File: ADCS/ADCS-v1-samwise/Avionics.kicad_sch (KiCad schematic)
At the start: 42 parts, among them SW1 KMR231NG LFS, SW2 KMR231NG LFS, U2 RP2350_80QFN, U3 MR25H40MDF, Y1 ABM8-272-T3

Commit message: ver 1.5
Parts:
- removed D4: LED, LED_SMD:LED_0603_1608Metric, symbol Device:LED
- removed TP13: TestPoint, TestPoint:TestPoint_Pad_D1.0mm, symbol Connector:TestPoint
- added D5: GREEN LED, LED_SMD:LED_0603_1608Metric, symbol Device:LED
- R70: value 650 -> 10k
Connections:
- net GND: now also D5.1 (K)
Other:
- note removed: "Vwd: 2V Ifwd: 2mA R = (3.3-2)/2mA = 650Ω"
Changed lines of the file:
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@@
 		(title "ADCS Main Board")
 		(date "2025-05-21")
-		(rev "1.4")
+		(rev "1.5")
 		(company "Stanford Student Space Initiative")
 		(comment 1 "Sage Wu")
@@
 		)
 	)
-	(text "Vwd: 2V\nIfwd: 2mA\nR = (3.3-2)/2mA\n= 650Ω"
-		(exclude_from_sim no)
-		(at 53.848 37.338 0)
-		(effects
-			(font
-				(size 1.27 1.27)
-			)
-			(justify left)
-		)
-	)
 	(text "capacitor for every power pin\n"
 		(exclude_from_sim no)
@@
 	)
 	(junction
+		(at 67.31 60.96)
+		(diameter 0)
+		(color 0 0 0 0)
+	)
+	(junction
 		(at 158.75 54.61)
 		(diameter 0)
@@
 	(wire
 		(pts
-			(xy 67.31 62.23) (xy 67.31 59.69)
+			(xy 67.31 62.23) (xy 67.31 60.96)
 		)
 		(stroke
@@
 	(wire
 		(pts
-			(xy 102.87 46.99) (xy 102.87 54.61)
-		)
-		(stroke
-			(width 0)
-			(type default)
-		)
-	)
-	(wire
-		(pts
 			(xy 143.51 158.75) (xy 147.32 158.75)
 		)
@@
 	(wire
 		(pts
+			(xy 67.31 60.96) (xy 67.31 59.69)
+		)
+		(stroke
+			(width 0)
+			(type default)
+		)
+	)
+	(wire
+		(pts
 			(xy 69.85 156.21) (xy 74.93 156.21)
 		)
@@
 	(wire
 		(pts
+			(xy 102.87 46.99) (xy 102.87 54.61)
+		)
+		(stroke
+			(width 0)
+			(type default)
+		)
+	)
+	(wire
+		(pts
 			(xy 143.51 143.51) (xy 147.32 143.51)
 		)
@@
 		)
 	)
+	(global_label "3V3_TEST"
+		(shape bidirectional)
+		(at 102.87 46.99 180)
+		(fields_autoplaced yes)
+		(effects
+			(font
+				(size 1.27 1.27)
+			)
+			(justify right)
+		)
+		(property "Intersheetrefs" "${INTERSHEET_REFS}"
+			(at 90.8176 46.99 0)
+			(effects
+				(font
+					(size 1.27 1.27)
+				)
+				(justify right)
+				(hide yes)
+			)
+		)
+	)
 	(global_label "pd_z+_1"
 		(shape input)
@@
 	)
 	(symbol
+		(lib_id "Device:LED")
+		(at 67.31 57.15 270)
+		(mirror x)
+		(unit 1)
+		(exclude_from_sim no)
+		(in_bom yes)
+		(on_board yes)
+		(dnp no)
+		(property "Reference" "D5"
+			(at 72.4154 57.3278 0)
+			(effects
+				(font
+					(size 1.27 1.27)
+				)
+			)
+		)
+		(property "Value" "GREEN LED"
+			(at 70.3072 57.3278 0)
+			(effects
+				(font
+					(size 0.9906 0.9906)
+				)
+			)
+		)
+		(property "Footprint" "LED_SMD:LED_0603_1608Metric"
+			(at 67.31 57.15 0)
+			(effects
+				(font
+					(size 1.27 1.27)
+				)
+				(hide yes)
+			)
+		)
+		(property "Datasheet" "https://optoelectronics.liteon.com/upload/download/DS22-2000-074/LTST-C190KGKT.PDF"
+			(at 67.31 57.15 0)
+			(effects
+				(font
+					(size 1.27 1.27)
+				)
+				(hide yes)
+			)
+		)
+		(property "Description" "Green LED"
+			(at 67.31 57.15 0)
+			(effects
+				(font
+					(size 1.27 1.27)
+				)
+				(hide yes)
+			)
+		)
+		(property "Flight" "LTST-C190KGKT"
+			(at 67.31 57.15 0)
+			(effects
+				(font
+					(size 1.27 1.27)
+				)
+				(hide yes)
+			)
+		)
+		(property "Manufacturer_Name" "Lite-On Inc."
+			(at 67.31 57.15 0)
+			(effects
+				(font
+					(size 1.27 1.27)
+				)
+				(hide yes)
+			)
+		)
+		(property "Manufacturer_Part_Number" "LTST-C190KGKT"
+			(at 74.9554 57.3278 0)
+			(effects
+				(font
+					(size 1.27 1.27)
+				)
+				(hide yes)
+			)
+		)
+		(property "Proto" "LTST-C190KGKT"
+			(at 67.31 57.15 0)
+			(effects
+				(font
+					(size 1.27 1.27)
+				)
+				(hide yes)
+			)
+		)
+		(property "Sim.Pins" "1=K 2=A"
+			(at 67.31 57.15 0)
+			(effects
+				(font
+					(size 1.27 1.27)
+				)
+			)
+		)
+		(pin "1"
+		)
+		(pin "2"
+		)
+		(instances
+			(project "ADCS_board"
+				(path "/db20b18b-d25a-428e-8229-70a189e1de75/00000000-0000-0000-0000-00005cec5a72"
+					(reference "D5")
+					(unit 1)
+				)
+			)
+		)
+	)
+	(symbol
 		(lib_id "Device:C_Small")
 		(at 34.29 100.33 0)
@@
 	)
 	(symbol
-		(lib_id "Connector:TestPoint")
-		(at 102.87 46.99 0)
-		(unit 1)
-		(exclude_from_sim no)
-		(in_bom no)
-		(on_board yes)
-		(dnp no)
-		(fields_autoplaced yes)
-		(property "Reference" "TP13"
-			(at 105.41 42.4179 0)
-			(effects
-				(font
-					(size 1.27 1.27)
-				)
-				(justify left)
-			)
-		)
-		(property "Value" "TestPoint"
-			(at 105.41 44.9579 0)
-			(effects
-				(font
-					(size 1.27 1.27)
-				)
-				(justify left)
-			)
-		)
-		(property "Footprint" "TestPoint:TestPoint_Pad_D1.0mm"
-			(at 107.95 46.99 0)
-			(effects
-				(font
-					(size 1.27 1.27)
-				)
-				(hide yes)
-			)
-		)
-		(property "Datasheet" "~"
-			(at 107.95 46.99 0)
-			(effects
-				(font
-					(size 1.27 1.27)
-				)
-				(hide yes)
-			)
-		)
-		(property "Description" "test point"
-			(at 102.87 46.99 0)
-			(effects
-				(font
-					(size 1.27 1.27)
-				)
-				(hide yes)
-			)
-		)
-		(pin "1"
-		)
-		(instances
-			(project "ADCS_board"
-				(path "/db20b18b-d25a-428e-8229-70a189e1de75/00000000-0000-0000-0000-00005cec5a72"
-					(reference "TP13")
-					(unit 1)
-				)
-			)
-		)
-	)
-	(symbol
 		(lib_id "Device:R_US")
 		(at 43.18 193.04 90)
@@
 			)
 		)
-		(property "Value" "650"
+		(property "Value" "10k"
 			(at 69.85 49.5299 0)
 			(effects
@@
 					(unit 1)
 				)
-			)
-		)
-	)
-	(symbol
-		(lib_id "Device:LED")
-		(at 67.31 55.88 90)
-		(unit 1)
-		(exclude_from_sim no)
-		(in_bom yes)
-		(on_board yes)
-		(dnp no)
-		(fields_autoplaced yes)
-		(property "Reference" "D4"
-			(at 71.12 56.1974 90)
-			(effects
-				(font
-					(size 1.27 1.27)
-				)
-				(justify right)
-			)
-		)
-		(property "Value" "LED"
-			(at 71.12 58.7374 90)
-			(effects
-				(font
-					(size 1.27 1.27)
-				)
-				(justify right)
-			)
-		)
-		(property "Footprint" "LED_SMD:LED_0603_1608Metric"
-			(at 67.31 55.88 0)
-			(effects
-				(font
-					(size 1.27 1.27)
-				)
-				(hide yes)
-			)
-		)
-		(property "Datasheet" "~"
-			(at 67.31 55.88 0)
-			(effects
-				(font
-					(size 1.27 1.27)
-				)
-				(hide yes)
-			)
-		)
-		(property "Description" "Light emitting diode"
-			(at 67.31 55.88 0)
-			(effects
-				(font
-					(size 1.27 1.27)
-				)
-				(hide yes)
-			)
-		)
-		(property "Sim.Pins" "1=K 2=A"
-			(at 67.31 55.88 0)
-			(effects
-				(font
-					(size 1.27 1.27)
-				)
-				(hide yes)
-			)
-		)
-		(pin "1"
-		)
-		(pin "2"
-		)
-		(instances
-			(project ""
-				(path "/db20b18b-d25a-428e-8229-70a189e1de75/00000000-0000-0000-0000-00005cec5a72"
-					(reference "D4")
-					(unit 1)
-				)

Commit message: ADCS v1.7
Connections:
- net at D5.2 (A): now also R70.1
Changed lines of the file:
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@@
 		(title "ADCS Main Board")
 		(date "2025-05-22")
-		(rev "1.6")
+		(rev "1.7")
 		(company "Stanford Student Space Initiative")
 		(comment 1 "Sage Wu")
@@
 	)
 	(junction
-		(at 67.31 60.96)
-		(diameter 0)
-		(color 0 0 0 0)
-	)
-	(junction
 		(at 158.75 54.61)
 		(diameter 0)
@@
 	(wire
 		(pts
+			(xy 67.31 60.96) (xy 67.31 63.5)
+		)
+		(stroke
+			(width 0)
+			(type default)
+		)
+	)
+	(wire
+		(pts
 			(xy 364.49 66.04) (xy 364.49 58.42)
 		)
@@
 	(wire
 		(pts
-			(xy 67.31 62.23) (xy 67.31 60.96)
-		)
-		(stroke
-			(width 0)
-			(type default)
-		)
-	)
-	(wire
-		(pts
 			(xy 118.11 80.01) (xy 120.65 80.01)
 		)
@@
 	(wire
 		(pts
-			(xy 80.01 38.1) (xy 80.01 41.91)
-		)
-		(stroke
-			(width 0)
-			(type default)
-		)
-	)
-	(wire
-		(pts
 			(xy 74.93 99.06) (xy 63.5 99.06)
 		)
@@
 	(wire
 		(pts
-			(xy 67.31 60.96) (xy 67.31 59.69)
-		)
-		(stroke
-			(width 0)
-			(type default)
-		)
-	)
-	(wire
-		(pts
 			(xy 69.85 156.21) (xy 74.93 156.21)
 		)
@@
 	(wire
 		(pts
+			(xy 80.01 35.56) (xy 80.01 41.91)
+		)
+		(stroke
+			(width 0)
+			(type default)
+		)
+	)
+	(wire
+		(pts
 			(xy 323.85 116.84) (xy 323.85 114.3)
 		)
@@
 	(wire
 		(pts
+			(xy 67.31 52.07) (xy 67.31 53.34)
+		)
+		(stroke
+			(width 0)
+			(type default)
+		)
+	)
+	(wire
+		(pts
 			(xy 336.55 173.99) (xy 336.55 177.8)
 		)
@@
 		)
 	)
-	(global_label "3V3_TEST"
+	(global_label "3.3V"
 		(shape bidirectional)
 		(at 102.87 46.99 180)
@@
 		)
 		(property "Intersheetrefs" "${INTERSHEET_REFS}"
-			(at 90.8176 46.99 0)
+			(at 95.4741 46.99 0)
 			(effects
 				(font
@@
 			)
 		)
-		(property "Datasheet" "https://optoelectronics.liteon.com/upload/download/DS22-2000-074/LTST-C190KGKT.PDF"
+		(property "Datasheet" "~"
 			(at 67.31 57.15 0)
 			(effects
@@
 			)
 		)
-		(property "Description" "Green LED"
+		(property "Description" "Light emitting diode"
 			(at 67.31 57.15 0)
 			(effects
@@
 		)
 		(property "Sim.Pins" "1=K 2=A"
-			(at 67.31 57.15 0)
+			(at 64.77 55.118 0)
 			(effects
 				(font
@@
 	(symbol
 		(lib_id "power:+3.3V")
-		(at 80.01 38.1 0)
+		(at 80.01 35.56 0)
 		(unit 1)
 		(exclude_from_sim no)
@@
 		(fields_autoplaced yes)
 		(property "Reference" "#P+04"
-			(at 80.01 38.1 0)
+			(at 80.01 35.56 0)
 			(effects
 				(font
@@
 		)
 		(property "Value" "3.3V"
-			(at 80.01 33.02 0)
+			(at 80.01 30.48 0)
 			(effects
 				(font
@@
 		)
 		(property "Footprint" ""
-			(at 80.01 38.1 0)
+			(at 80.01 35.56 0)
 			(effects
 				(font
@@
 		)
 		(property "Datasheet" ""
-			(at 80.01 38.1 0)
+			(at 80.01 35.56 0)
 			(effects
 				(font
@@
 		)
 		(property "Description" "Power symbol creates a global label with name \"+3.3V\""
-			(at 80.01 38.1 0)
+			(at 80.01 35.56 0)
 			(effects
 				(font
@@
 	(symbol
 		(lib_id "power:GND")
-		(at 67.31 62.23 0)
+		(at 67.31 63.5 0)
 		(unit 1)
 		(exclude_from_sim no)
@@
 		(fields_autoplaced yes)
 		(property "Reference" "#PWR088"
-			(at 67.31 68.58 0)
+			(at 67.31 69.85 0)
 			(effects
 				(font
@@
 		)
 		(property "Value" "GND"
-			(at 67.31 67.31 0)
+			(at 67.31 68.58 0)
 			(effects
 				(font
@@
 		)
 		(property "Footprint" ""
-			(at 67.31 62.23 0)
+			(at 67.31 63.5 0)
 			(effects
 				(font
@@
 		)
 		(property "Datasheet" ""
-			(at 67.31 62.23 0)
+			(at 67.31 63.5 0)
 			(effects
 				(font
@@
 		)
 		(property "Description" "Power symbol creates a global label with name \"GND\" , ground"
-			(at 67.31 62.23 0)
+			(at 67.31 63.5 0)
 			(effects
 				(font

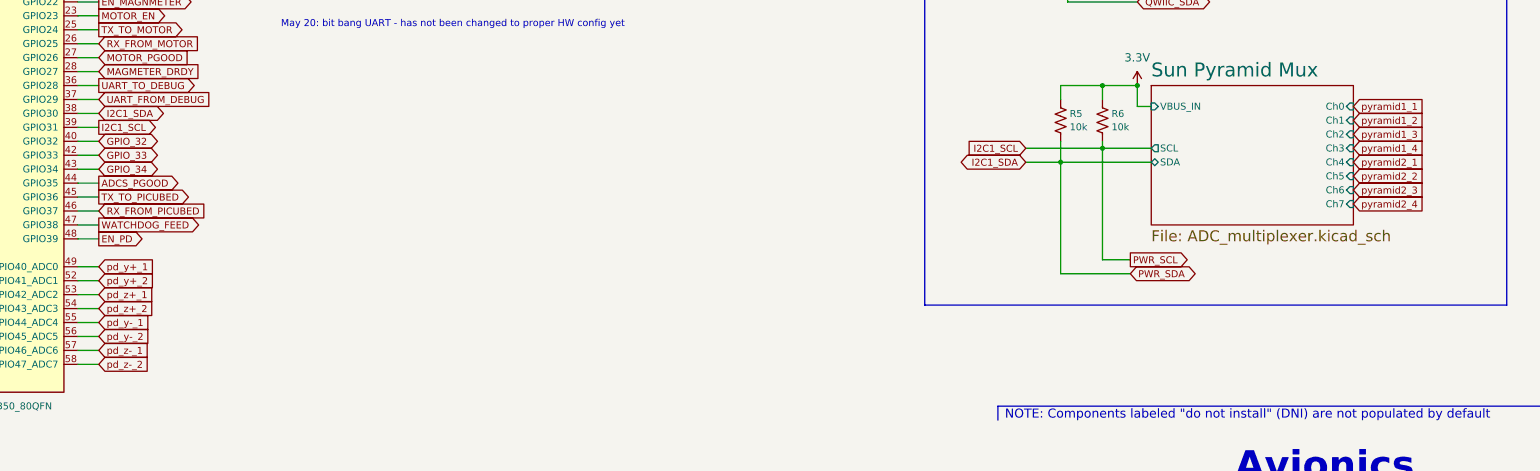
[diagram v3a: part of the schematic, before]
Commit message: Swap sun pyramid / photodiode yz inputs
Swap sun pyramid / photodiode yz inputs
 - Sun pyramids (8) -> RP3250B ADC pins
 - Photodiode yz (8) -> ADS7830 ADC
 - Logic behind this: RP2350B ADC has higher fidelity than ADS7830, and the yz photodiodes point in redundant directions so that's a waste.
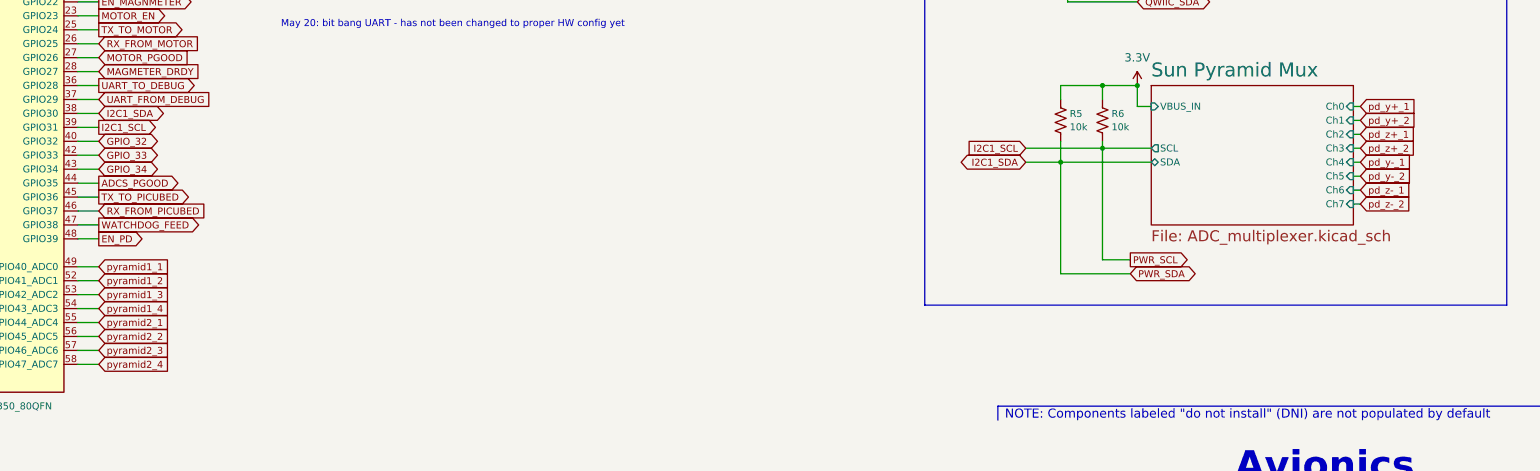
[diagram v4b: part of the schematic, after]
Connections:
- net pd_y+_1: no longer U2.49 (GPIO40_ADC0)
- net pd_y+_2: no longer U2.52 (GPIO41_ADC1)
- net pd_y-_1: no longer U2.55 (GPIO44_ADC4)
- net pd_y-_2: no longer U2.56 (GPIO45_ADC5)
- net pd_z+_1: no longer U2.53 (GPIO42_ADC2)
- net pd_z+_2: no longer U2.54 (GPIO43_ADC3)
- net pd_z-_1: no longer U2.57 (GPIO46_ADC6)
- net pd_z-_2: no longer U2.58 (GPIO47_ADC7)
- net pyramid1_1: now also U2.49 (GPIO40_ADC0)
- net pyramid1_2: now also U2.52 (GPIO41_ADC1)
- net pyramid1_3: now also U2.53 (GPIO42_ADC2)
- net pyramid1_4: now also U2.54 (GPIO43_ADC3)
- net pyramid2_1: now also U2.55 (GPIO44_ADC4)
- net pyramid2_2: now also U2.56 (GPIO45_ADC5)
- net pyramid2_3: now also U2.57 (GPIO46_ADC6)
- net pyramid2_4: now also U2.58 (GPIO47_ADC7)

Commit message: Revert "Swap sun pyramid / photodiode yz inputs"
This reverts commit 476f3e609712227db83ea3ec49a2480c44b72f0a.
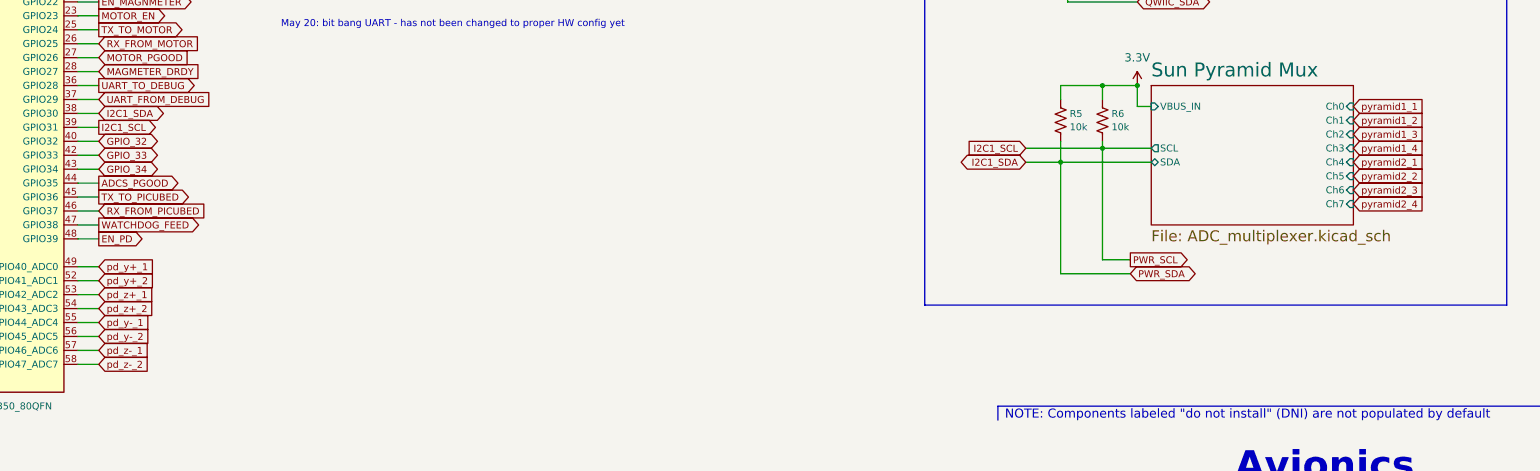
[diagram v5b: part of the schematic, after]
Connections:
- net pd_y+_1: now also U2.49 (GPIO40_ADC0)
- net pd_y+_2: now also U2.52 (GPIO41_ADC1)
- net pd_y-_1: now also U2.55 (GPIO44_ADC4)
- net pd_y-_2: now also U2.56 (GPIO45_ADC5)
- net pd_z+_1: now also U2.53 (GPIO42_ADC2)
- net pd_z+_2: now also U2.54 (GPIO43_ADC3)
- net pd_z-_1: now also U2.57 (GPIO46_ADC6)
- net pd_z-_2: now also U2.58 (GPIO47_ADC7)
- net pyramid1_1: no longer U2.49 (GPIO40_ADC0)
- net pyramid1_2: no longer U2.52 (GPIO41_ADC1)
- net pyramid1_3: no longer U2.53 (GPIO42_ADC2)
- net pyramid1_4: no longer U2.54 (GPIO43_ADC3)
- net pyramid2_1: no longer U2.55 (GPIO44_ADC4)
- net pyramid2_2: no longer U2.56 (GPIO45_ADC5)
- net pyramid2_3: no longer U2.57 (GPIO46_ADC6)
- net pyramid2_4: no longer U2.58 (GPIO47_ADC7)

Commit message: Sun sensor fixes (schematic)
1. Swap sun pyramid / photodiode yz inputs
 - Sun pyramids (8) -> RP3250B ADC pins
 - Photodiode yz (8) -> ADS7830 ADC
 - Logic behind this: RP2350B ADC has higher fidelity than ADS7830, and the yz photodiodes point in redundant directions so that's a waste.

2. Add 3.3v reference voltage to ADS7830
 - V_REF_RP2350B_ADC = 3.3v (can't change), V_REF_ADS7830 = 2.5v (internal)
 - This requires us to clip readings from the RP2350B ADC in the code
 - Since the ADS7830 can accept an external reference voltage, I've connected it up to the 3.3v bus to circumvent those reading issues :)

referenced adafruit ads7830 breakout board circuit for edits (link)[https://github.com/adafruit/Adafruit-ADS7830-PCB/tree/main]
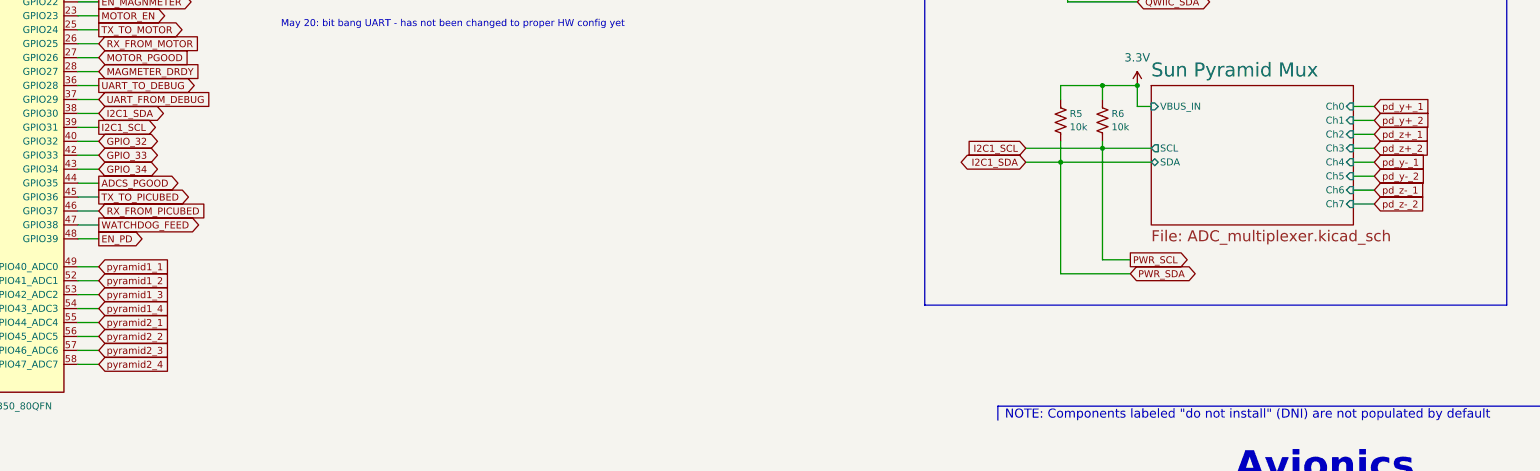
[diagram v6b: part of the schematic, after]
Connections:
- net pd_y+_1: no longer U2.49 (GPIO40_ADC0)
- net pd_y+_2: no longer U2.52 (GPIO41_ADC1)
- net pd_y-_1: no longer U2.55 (GPIO44_ADC4)
- net pd_y-_2: no longer U2.56 (GPIO45_ADC5)
- net pd_z+_1: no longer U2.53 (GPIO42_ADC2)
- net pd_z+_2: no longer U2.54 (GPIO43_ADC3)
- net pd_z-_1: no longer U2.57 (GPIO46_ADC6)
- net pd_z-_2: no longer U2.58 (GPIO47_ADC7)
- net pyramid1_1: now also U2.49 (GPIO40_ADC0)
- net pyramid1_2: now also U2.52 (GPIO41_ADC1)
- net pyramid1_3: now also U2.53 (GPIO42_ADC2)
- net pyramid1_4: now also U2.54 (GPIO43_ADC3)
- net pyramid2_1: now also U2.55 (GPIO44_ADC4)
- net pyramid2_2: now also U2.56 (GPIO45_ADC5)
- net pyramid2_3: now also U2.57 (GPIO46_ADC6)
- net pyramid2_4: now also U2.58 (GPIO47_ADC7)
